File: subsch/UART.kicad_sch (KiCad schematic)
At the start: 2 parts

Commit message: USB2UART
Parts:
- C1: renamed from C24; value (none) -> ~; footprint (none) -> Capacitor_SMD:C_0603_1608Metric
- U1: renamed from U7; value (none) -> ~; footprint (none) -> Package_SO:MSOP-10_3x3mm_P0.5mm
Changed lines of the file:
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@@
     (effects (font (size 1.27 1.27)) (justify left))
   )
-  (symbol (lib_id "Device:C_Small") (at 116.332 85.598 0) (mirror y) (unit 1)
+  (symbol (lib_id "Device:C_Small") (at 116.332 85.598 0) (mirror y)
     (in_bom yes) (on_board yes)
-    (property "Reference" "C24" (id 0) (at 117.602 83.566 0)
+    (property "Reference" "C1" (id 0) (at 117.602 83.566 0)
       (effects (font (size 1.27 1.27)) (justify right))
     )
-    (property "Value" "" (id 1) (at 117.348 88.138 0)
+    (property "Value" "~" (id 1) (at 117.348 88.138 0)
       (effects (font (size 1.27 1.27)) (justify right))
     )
-    (property "Footprint" "" (id 2) (at 116.332 85.598 0)
+    (property "Footprint" "Capacitor_SMD:C_0603_1608Metric" (id 2) (at 116.332 85.598 0)
       (effects (font (size 1.27 1.27)) hide)
     )
@@
     (pin "2")
   )
-  (symbol (lib_id "power:GND") (at 116.332 90.17 0) (unit 1)
+  (symbol (lib_id "power:GND") (at 116.332 90.17 0)
     (in_bom yes) (on_board yes) (fields_autoplaced)
-    (property "Reference" "#PWR075" (id 0) (at 116.332 96.52 0)
+    (property "Reference" "#PWR0107" (id 0) (at 116.332 96.52 0)
       (effects (font (size 1.27 1.27)) hide)
     )
-    (property "Value" "" (id 1) (at 116.332 94.7325 0))
+    (property "Value" "~" (id 1) (at 116.332 94.7325 0))
     (property "Footprint" "" (id 2) (at 116.332 90.17 0)
       (effects (font (size 1.27 1.27)) hide)
@@
     (pin "1")
   )
-  (symbol (lib_id "Interface_USB:CH340E") (at 141.478 87.63 0) (unit 1)
+  (symbol (lib_id "Interface_USB:CH340E") (at 141.478 87.63 0)
     (in_bom yes) (on_board yes) (fields_autoplaced)
-    (property "Reference" "U7" (id 0) (at 143.4974 102.4795 0)
+    (property "Reference" "U1" (id 0) (at 143.4974 102.4795 0)
       (effects (font (size 1.27 1.27)) (justify left))
     )
-    (property "Value" "" (id 1) (at 143.4974 105.2546 0)
+    (property "Value" "~" (id 1) (at 143.4974 105.2546 0)
       (effects (font (size 1.27 1.27)) (justify left))
     )
-    (property "Footprint" "" (id 2) (at 142.748 101.6 0)
+    (property "Footprint" "Package_SO:MSOP-10_3x3mm_P0.5mm" (id 2) (at 142.748 101.6 0)
       (effects (font (size 1.27 1.27)) (justify left) hide)
     )
@@
     (pin "9")
   )
-  (symbol (lib_id "power:VCC") (at 116.332 81.534 0) (unit 1)
+  (symbol (lib_id "power:VCC") (at 116.332 81.534 0)
     (in_bom yes) (on_board yes) (fields_autoplaced)
-    (property "Reference" "#PWR074" (id 0) (at 116.332 85.344 0)
+    (property "Reference" "#PWR0108" (id 0) (at 116.332 85.344 0)
       (effects (font (size 1.27 1.27)) hide)
     )
-    (property "Value" "" (id 1) (at 116.332 77.9295 0))
+    (property "Value" "~" (id 1) (at 116.332 77.9295 0))
     (property "Footprint" "" (id 2) (at 116.332 81.534 0)
       (effects (font (size 1.27 1.27)) hide)
@@
     (pin "1")
   )
-  (symbol (lib_id "power:GND") (at 141.478 104.394 0) (unit 1)
+  (symbol (lib_id "power:GND") (at 141.478 104.394 0)
     (in_bom yes) (on_board yes) (fields_autoplaced)
-    (property "Reference" "#PWR076" (id 0) (at 141.478 110.744 0)
+    (property "Reference" "#PWR0105" (id 0) (at 141.478 110.744 0)
       (effects (font (size 1.27 1.27)) hide)
     )
-    (property "Value" "" (id 1) (at 141.478 108.9565 0))
+    (property "Value" "~" (id 1) (at 141.478 108.9565 0))
     (property "Footprint" "" (id 2) (at 141.478 104.394 0)
       (effects (font (size 1.27 1.27)) hide)
@@
     (pin "1")
   )
-  (symbol (lib_id "power:VCC") (at 138.938 69.85 0) (unit 1)
+  (symbol (lib_id "power:VCC") (at 138.938 69.85 0)
     (in_bom yes) (on_board yes) (fields_autoplaced)
-    (property "Reference" "#PWR073" (id 0) (at 138.938 73.66 0)
+    (property "Reference" "#PWR0106" (id 0) (at 138.938 73.66 0)
       (effects (font (size 1.27 1.27)) hide)
     )
-    (property "Value" "" (id 1) (at 138.938 66.2455 0))
+    (property "Value" "~" (id 1) (at 138.938 66.2455 0))
     (property "Footprint" "" (id 2) (at 138.938 69.85 0)
       (effects (font (size 1.27 1.27)) hide)

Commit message: another right version
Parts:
- renumbered C1 to C24, U1 to U7
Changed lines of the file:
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@@
   (symbol (lib_id "Device:C_Small") (at 116.332 85.598 0) (mirror y)
     (in_bom yes) (on_board yes)
-    (property "Reference" "C1" (id 0) (at 117.602 83.566 0)
+    (property "Reference" "C24" (id 0) (at 117.602 83.566 0)
       (effects (font (size 1.27 1.27)) (justify right))
     )
@@
   (symbol (lib_id "power:GND") (at 116.332 90.17 0)
     (in_bom yes) (on_board yes) (fields_autoplaced)
-    (property "Reference" "#PWR0107" (id 0) (at 116.332 96.52 0)
+    (property "Reference" "#PWR075" (id 0) (at 116.332 96.52 0)
       (effects (font (size 1.27 1.27)) hide)
     )
@@
   (symbol (lib_id "Interface_USB:CH340E") (at 141.478 87.63 0)
     (in_bom yes) (on_board yes) (fields_autoplaced)
-    (property "Reference" "U1" (id 0) (at 143.4974 102.4795 0)
+    (property "Reference" "U7" (id 0) (at 143.4974 102.4795 0)
       (effects (font (size 1.27 1.27)) (justify left))
     )
@@
   (symbol (lib_id "power:VCC") (at 116.332 81.534 0)
     (in_bom yes) (on_board yes) (fields_autoplaced)
-    (property "Reference" "#PWR0108" (id 0) (at 116.332 85.344 0)
+    (property "Reference" "#PWR074" (id 0) (at 116.332 85.344 0)
       (effects (font (size 1.27 1.27)) hide)
     )
@@
   (symbol (lib_id "power:GND") (at 141.478 104.394 0)
     (in_bom yes) (on_board yes) (fields_autoplaced)
-    (property "Reference" "#PWR0105" (id 0) (at 141.478 110.744 0)
+    (property "Reference" "#PWR076" (id 0) (at 141.478 110.744 0)
       (effects (font (size 1.27 1.27)) hide)
     )
@@
   (symbol (lib_id "power:VCC") (at 138.938 69.85 0)
     (in_bom yes) (on_board yes) (fields_autoplaced)
-    (property "Reference" "#PWR0106" (id 0) (at 138.938 73.66 0)
+    (property "Reference" "#PWR073" (id 0) (at 138.938 73.66 0)
       (effects (font (size 1.27 1.27)) hide)
     )

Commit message: iterative optimization
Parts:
- C1: renamed from C24; value ~ -> 100n
- U1: renamed from U7; value ~ -> CH340E
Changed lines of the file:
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@@
   (symbol (lib_id "Device:C_Small") (at 116.332 85.598 0) (mirror y)
     (in_bom yes) (on_board yes)
-    (property "Reference" "C24" (id 0) (at 117.602 83.566 0)
+    (property "Reference" "C1" (id 0) (at 117.602 83.566 0)
       (effects (font (size 1.27 1.27)) (justify right))
     )
-    (property "Value" "~" (id 1) (at 117.348 88.138 0)
+    (property "Value" "100n" (id 1) (at 117.348 88.138 0)
       (effects (font (size 1.27 1.27)) (justify right))
     )
@@
   (symbol (lib_id "power:GND") (at 116.332 90.17 0)
     (in_bom yes) (on_board yes) (fields_autoplaced)
-    (property "Reference" "#PWR075" (id 0) (at 116.332 96.52 0)
+    (property "Reference" "#PWR0107" (id 0) (at 116.332 96.52 0)
       (effects (font (size 1.27 1.27)) hide)
     )
@@
   (symbol (lib_id "Interface_USB:CH340E") (at 141.478 87.63 0)
     (in_bom yes) (on_board yes) (fields_autoplaced)
-    (property "Reference" "U7" (id 0) (at 143.4974 102.4795 0)
+    (property "Reference" "U1" (id 0) (at 143.4974 102.4795 0)
       (effects (font (size 1.27 1.27)) (justify left))
     )
-    (property "Value" "~" (id 1) (at 143.4974 105.2546 0)
+    (property "Value" "CH340E" (id 1) (at 143.4974 105.2546 0)
       (effects (font (size 1.27 1.27)) (justify left))
     )
@@
   (symbol (lib_id "power:VCC") (at 116.332 81.534 0)
     (in_bom yes) (on_board yes) (fields_autoplaced)
-    (property "Reference" "#PWR074" (id 0) (at 116.332 85.344 0)
+    (property "Reference" "#PWR0108" (id 0) (at 116.332 85.344 0)
       (effects (font (size 1.27 1.27)) hide)
     )
@@
   (symbol (lib_id "power:GND") (at 141.478 104.394 0)
     (in_bom yes) (on_board yes) (fields_autoplaced)
-    (property "Reference" "#PWR076" (id 0) (at 141.478 110.744 0)
+    (property "Reference" "#PWR0105" (id 0) (at 141.478 110.744 0)
       (effects (font (size 1.27 1.27)) hide)
     )
@@
   (symbol (lib_id "power:VCC") (at 138.938 69.85 0)
     (in_bom yes) (on_board yes) (fields_autoplaced)
-    (property "Reference" "#PWR073" (id 0) (at 138.938 73.66 0)
+    (property "Reference" "#PWR0106" (id 0) (at 138.938 73.66 0)
       (effects (font (size 1.27 1.27)) hide)
     )

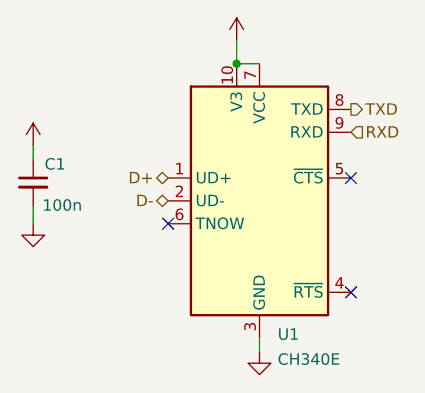
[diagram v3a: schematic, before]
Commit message: Change USB2XXX to USB2UART
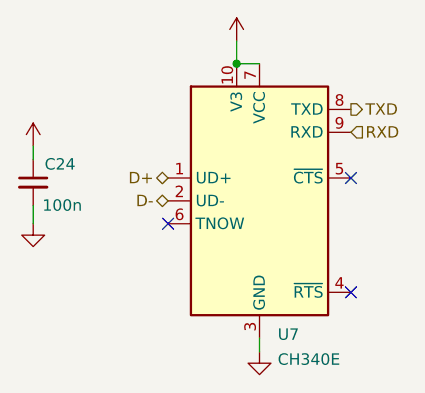
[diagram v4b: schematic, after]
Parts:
- renumbered C1 to C24, U1 to U7
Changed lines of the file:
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@@
   (symbol (lib_id "Device:C_Small") (at 116.332 85.598 0) (mirror y)
     (in_bom yes) (on_board yes)
-    (property "Reference" "C1" (id 0) (at 117.602 83.566 0)
+    (property "Reference" "C24" (id 0) (at 117.602 83.566 0)
       (effects (font (size 1.27 1.27)) (justify right))
     )
@@
   (symbol (lib_id "power:GND") (at 116.332 90.17 0)
     (in_bom yes) (on_board yes) (fields_autoplaced)
-    (property "Reference" "#PWR0107" (id 0) (at 116.332 96.52 0)
+    (property "Reference" "#PWR075" (id 0) (at 116.332 96.52 0)
       (effects (font (size 1.27 1.27)) hide)
     )
@@
   (symbol (lib_id "Interface_USB:CH340E") (at 141.478 87.63 0)
     (in_bom yes) (on_board yes) (fields_autoplaced)
-    (property "Reference" "U1" (id 0) (at 143.4974 102.4795 0)
+    (property "Reference" "U7" (id 0) (at 143.4974 102.4795 0)
       (effects (font (size 1.27 1.27)) (justify left))
     )
@@
   (symbol (lib_id "power:VCC") (at 116.332 81.534 0)
     (in_bom yes) (on_board yes) (fields_autoplaced)
-    (property "Reference" "#PWR0108" (id 0) (at 116.332 85.344 0)
+    (property "Reference" "#PWR074" (id 0) (at 116.332 85.344 0)
       (effects (font (size 1.27 1.27)) hide)
     )
@@
   (symbol (lib_id "power:GND") (at 141.478 104.394 0)
     (in_bom yes) (on_board yes) (fields_autoplaced)
-    (property "Reference" "#PWR0105" (id 0) (at 141.478 110.744 0)
+    (property "Reference" "#PWR076" (id 0) (at 141.478 110.744 0)
       (effects (font (size 1.27 1.27)) hide)
     )
@@
   (symbol (lib_id "power:VCC") (at 138.938 69.85 0)
     (in_bom yes) (on_board yes) (fields_autoplaced)
-    (property "Reference" "#PWR0106" (id 0) (at 138.938 73.66 0)
+    (property "Reference" "#PWR073" (id 0) (at 138.938 73.66 0)
       (effects (font (size 1.27 1.27)) hide)
     )
